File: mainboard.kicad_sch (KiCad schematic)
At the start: 0 parts

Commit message: schematic wip
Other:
- sheet CONTROL Port renamed USB
- added sheet Radio (radio.kicad_sch)
- sheet Clock and Miscellaneous ports: added AFE_CLK, FPGA_CLK, RX_MIX_CLK, RX_RCVR_CLK, TX_MIX_CLK, TX_XCVR_CLK; removed CLOCK_60MHZ
- sheet Debugger ports: added LED[1..3], MCU_D+, MCU_D-, USB_RESET_DETECT, USB_SWITCH; removed CONTROL_MCU_D+, CONTROL_MCU_D-, CONTROL_RESET_DETECT, CONTROL_SWITCH, LED[10..14]
- sheet Expansion Interfaces ports: added PMOD[1..10]; removed PMOD_A[0..7], PMOD_B[0..7]
- sheet FPGA Banks 0 and 1 ports: added 3V3RX_EN, AFE_ALT_CLK, AFE_SPI{SPI}, DA[0..7], DD[0..9], RX_MIX_CTRL{RFFC5072}, RX_RCVR{MAX2120}, ~{RX_MIX_BYPASS}; removed CLOCK_60MHZ, LED[0..5], MEZZANINE[1..30], PMOD_A[0..7], PMOD_B[0..7]
- sheet FPGA Banks 2 and 3 ports: added 3V3TX_EN, FPGA_CLK, LED[4..6], PHY{ULPI}, TX_MIX_CTRL{RFFC5072}, TX_XCVR{MAX2831}, ~{TX_MIX_BYPASS}; removed CONTROL_PHY{ULPI}, MEZZANINE[1..30], ~{BTN_USER}
- sheet FPGA Banks 6 and 7 ports: added MEZZANINE[1..30], PMOD[1..10], ~{BTN_USER}; removed none
- sheet LEDs and Buttons ports: added LED[1..3], LED[4..6]; removed LED[0..5], LED[10..14]
- sheet Power Supplies ports: added ~{POWER_GOOD}; removed none
- sheet USB: file control_port.kicad_sch -> usb.kicad_sch
- sheet USB ports: added MCU_D+, MCU_D-, PHY{ULPI}, USB_RESET_DETECT, USB_SWITCH; removed CONTROL_MCU_D+, CONTROL_MCU_D-, CONTROL_PHY{ULPI}, CONTROL_RESET_DETECT, CONTROL_SWITCH

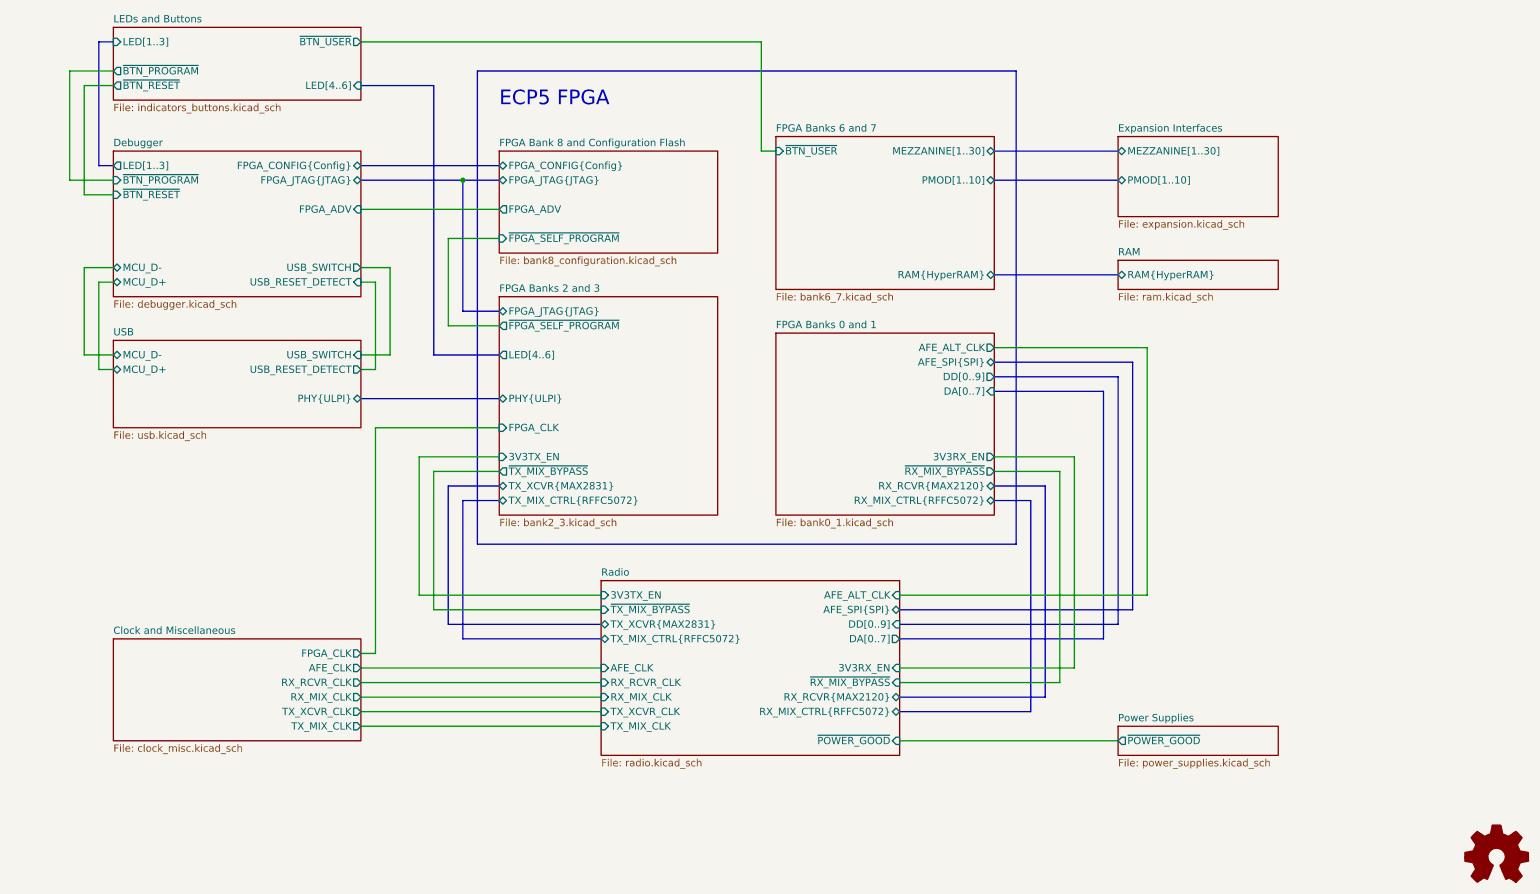
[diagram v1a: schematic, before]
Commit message: add regulator for analog 3.3 V supply
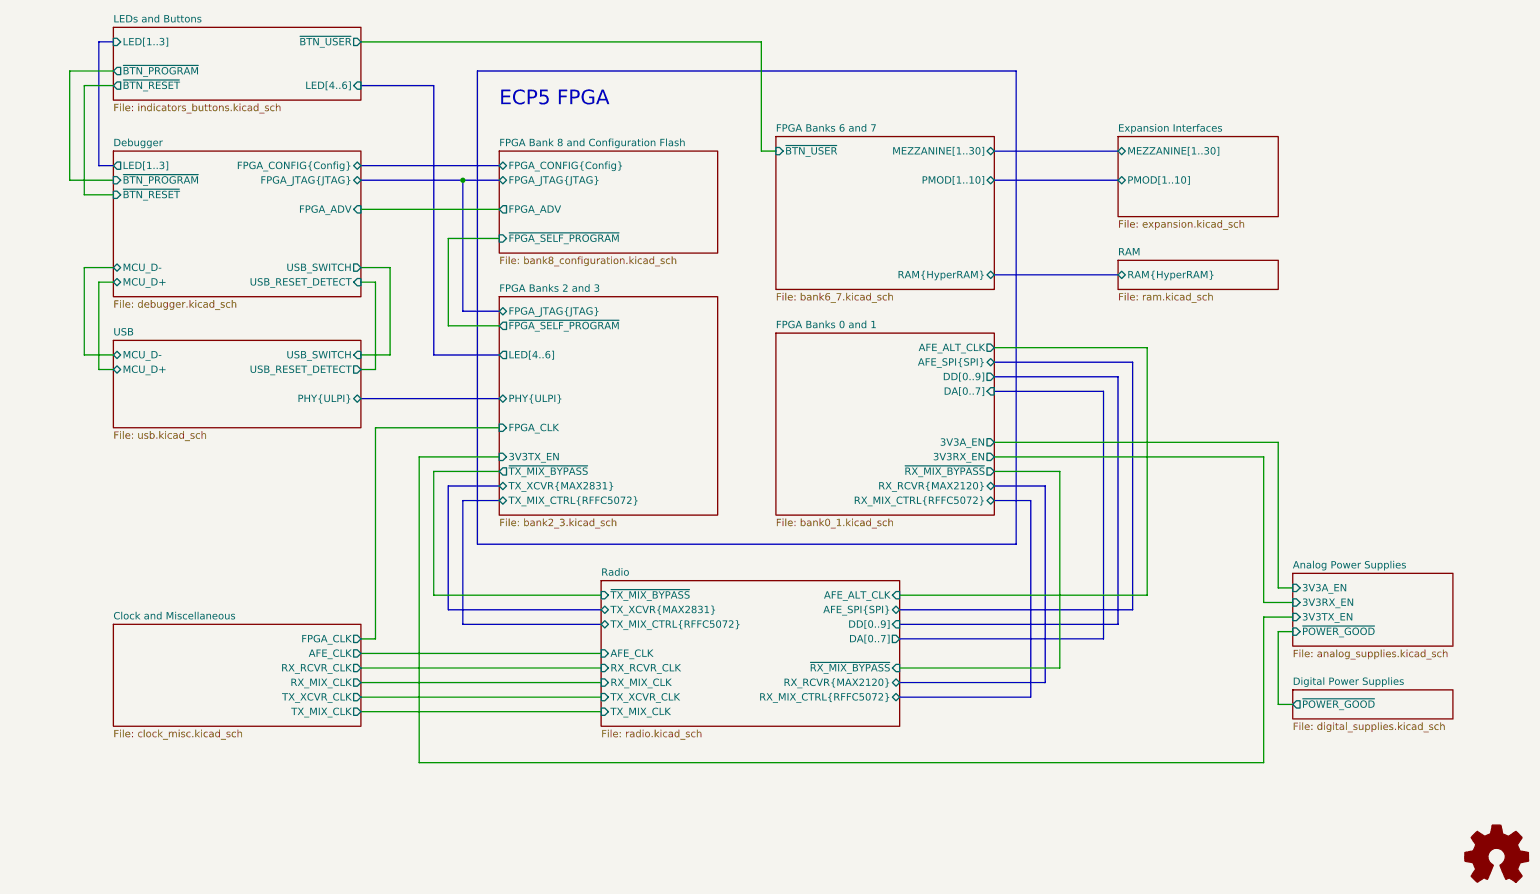
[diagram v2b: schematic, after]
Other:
- sheet Power Supplies renamed Digital Power Supplies
- added sheet Analog Power Supplies (analog_supplies.kicad_sch)
- sheet Digital Power Supplies: file power_supplies.kicad_sch -> digital_supplies.kicad_sch
- sheet FPGA Banks 0 and 1 ports: added 3V3A_EN; removed none
- sheet Radio ports: added none; removed 3V3RX_EN, 3V3TX_EN, ~{POWER_GOOD}

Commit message: complete initial layout
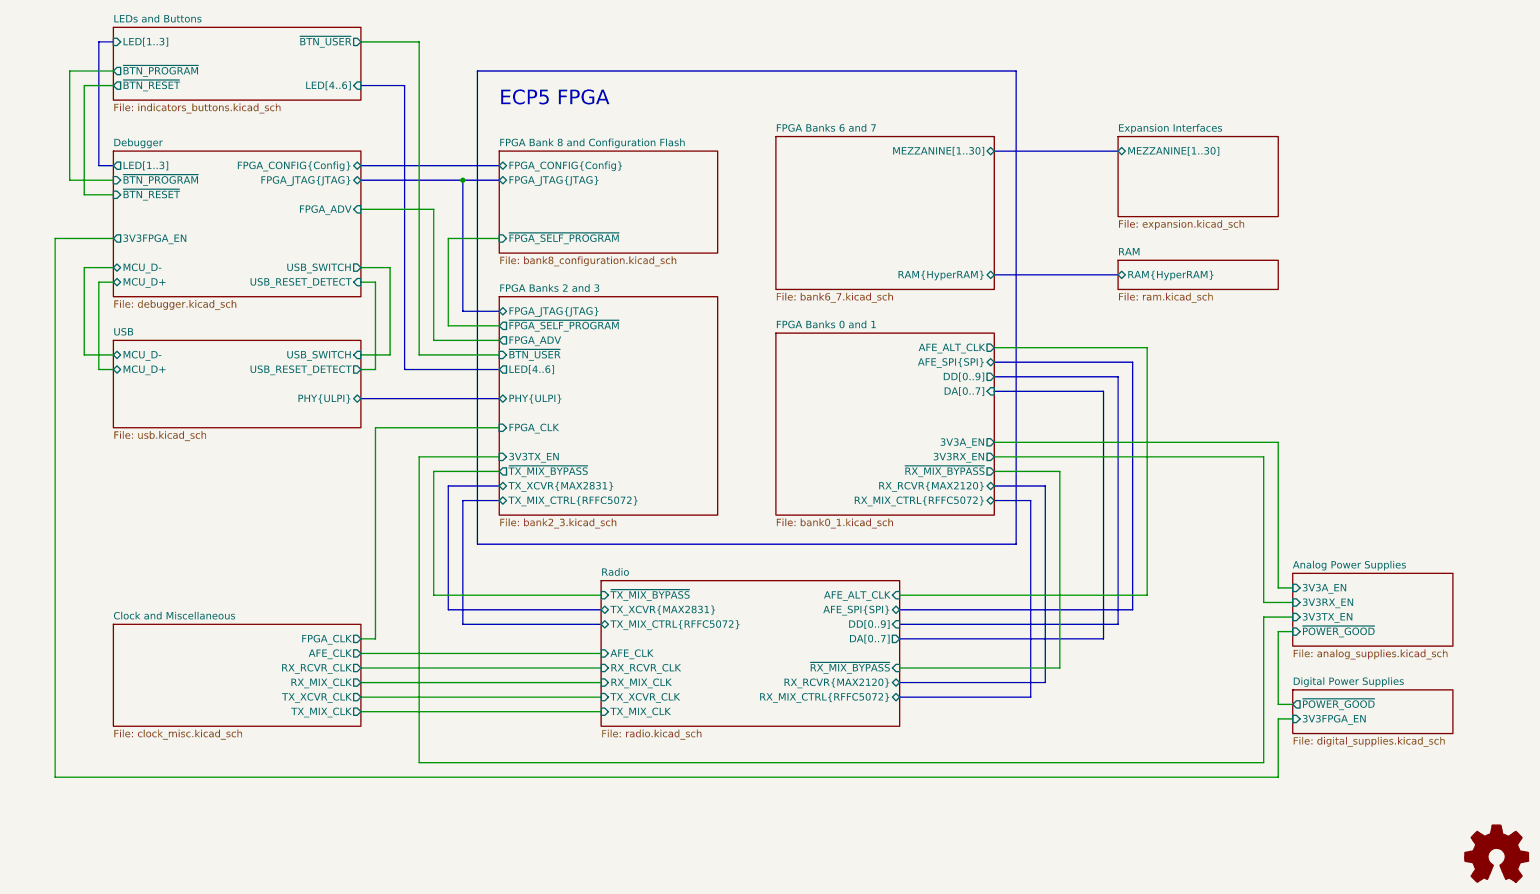
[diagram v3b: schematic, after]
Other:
- sheet Debugger ports: added 3V3FPGA_EN; removed none
- sheet Digital Power Supplies ports: added 3V3FPGA_EN; removed none
- sheet Expansion Interfaces ports: added none; removed PMOD[1..10]
- sheet FPGA Bank 8 and Configuration Flash ports: added none; removed FPGA_ADV
- sheet FPGA Banks 2 and 3 ports: added FPGA_ADV, ~{BTN_USER}; removed none
- sheet FPGA Banks 6 and 7 ports: added none; removed PMOD[1..10], ~{BTN_USER}
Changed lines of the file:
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@@
+    (stroke (width 0) (type default))
+  )
+  (wire (pts (xy 25.4 67.31) (xy 25.4 161.29))
     (stroke (width 0) (type default))
   )
@@
     (stroke (width 0) (type default))
   )
-  (wire (pts (xy 78.74 62.23) (xy 102.87 62.23))
-    (stroke (width 0) (type default))
-  )
   (bus (pts (xy 78.74 54.61) (xy 102.87 54.61))
     (stroke (width 0) (type default))
@@
     (stroke (width 0) (type default))
   )
+  (wire (pts (xy 78.74 33.02) (xy 88.9 33.02))
+    (stroke (width 0) (type default))
+  )
   (wire (pts (xy 189.23 107.95) (xy 200.66 107.95))
     (stroke (width 0) (type default))
   )
+  (wire (pts (xy 25.4 67.31) (xy 35.56 67.31))
+    (stroke (width 0) (type default))
+  )
   (wire (pts (xy 91.44 129.54) (xy 120.65 129.54))
     (stroke (width 0) (type default))
@@
     (stroke (width 0) (type default))
   )
+  (wire (pts (xy 91.44 62.23) (xy 78.74 62.23))
+    (stroke (width 0) (type default))
+  )
   (wire (pts (xy 33.02 74.93) (xy 33.02 90.17))
     (stroke (width 0) (type default))
@@
     (stroke (width 0) (type default))
   )
-  (wire (pts (xy 78.74 33.02) (xy 148.59 33.02))
-    (stroke (width 0) (type default))
-  )
   (bus (pts (xy 210.82 91.44) (xy 210.82 134.62))
     (stroke (width 0) (type default))
   )
+  (wire (pts (xy 238.76 161.29) (xy 25.4 161.29))
+    (stroke (width 0) (type default))
+  )
   (bus (pts (xy 93.98 132.08) (xy 120.65 132.08))
     (stroke (width 0) (type default))
   )
+  (wire (pts (xy 91.44 85.09) (xy 91.44 62.23))
+    (stroke (width 0) (type default))
+  )
   (bus (pts (xy 93.98 110.49) (xy 93.98 132.08))
     (stroke (width 0) (type default))
@@
     (stroke (width 0) (type default))
   )
+  (wire (pts (xy 241.3 151.13) (xy 238.76 151.13))
+    (stroke (width 0) (type default))
+  )
   (wire (pts (xy 189.23 105.41) (xy 236.22 105.41))
     (stroke (width 0) (type default))
@@
     (stroke (width 0) (type default))
   )
-  (bus (pts (xy 189.23 57.15) (xy 210.82 57.15))
-    (stroke (width 0) (type default))
-  )
   (wire (pts (xy 102.87 67.31) (xy 93.98 67.31))
     (stroke (width 0) (type default))
   )
-  (wire (pts (xy 148.59 33.02) (xy 148.59 52.07))
-    (stroke (width 0) (type default))
-  )
   (bus (pts (xy 213.36 88.9) (xy 213.36 132.08))
     (stroke (width 0) (type default))
@@
     (stroke (width 0) (type default))
   )
-  (bus (pts (xy 78.74 40.64) (xy 91.44 40.64))
-    (stroke (width 0) (type default))
-  )
-  (wire (pts (xy 148.59 52.07) (xy 151.13 52.07))
+  (wire (pts (xy 88.9 33.02) (xy 88.9 87.63))
+    (stroke (width 0) (type default))
+  )
+  (bus (pts (xy 78.74 40.64) (xy 86.36 40.64))
+    (stroke (width 0) (type default))
+  )
+  (wire (pts (xy 88.9 87.63) (xy 102.87 87.63))
     (stroke (width 0) (type default))
   )
@@
     (stroke (width 0) (type default))
   )
+  (wire (pts (xy 102.87 85.09) (xy 91.44 85.09))
+    (stroke (width 0) (type default))
+  )
   (wire (pts (xy 241.3 135.89) (xy 238.76 135.89))
     (stroke (width 0) (type default))
@@
     (stroke (width 0) (type default))
   )
-  (bus (pts (xy 102.87 87.63) (xy 91.44 87.63))
+  (bus (pts (xy 102.87 90.17) (xy 86.36 90.17))
     (stroke (width 0) (type default))
   )
@@
     (stroke (width 0) (type default))
   )
-  (bus (pts (xy 91.44 87.63) (xy 91.44 40.64))
+  (bus (pts (xy 86.36 90.17) (xy 86.36 40.64))
     (stroke (width 0) (type default))
   )
@@
   )
   (wire (pts (xy 78.74 142.24) (xy 120.65 142.24))
+    (stroke (width 0) (type default))
+  )
+  (wire (pts (xy 238.76 151.13) (xy 238.76 161.29))
     (stroke (width 0) (type default))
   )
@@
     )
   )
-  (sheet (at 241.3 146.05) (size 27.94 5.08) (fields_autoplaced)
+  (sheet (at 241.3 146.05) (size 27.94 7.62) (fields_autoplaced)
     (stroke (width 0) (type solid))
     (fill (color 0 0 0 0.0000))
@@
       (effects (font (size 1.27 1.27)) (justify left bottom))
     )
-    (property "Sheetfile" "digital_supplies.kicad_sch" (at 241.3 151.7146 0)
+    (property "Sheetfile" "digital_supplies.kicad_sch" (at 241.3 154.2546 0)
       (effects (font (size 1.27 1.27)) (justify left top))
     )
@@
       (effects (font (size 1.27 1.27)) (justify left))
     )
+    (pin "3V3FPGA_EN" input (at 241.3 151.13 180)
+      (effects (font (size 1.27 1.27)) (justify left))
+    )
     (instances
       (project "mainboard"
@@
     )
     (pin "LED[1..3]" output (at 35.56 54.61 180)
+      (effects (font (size 1.27 1.27)) (justify left))
+    )
+    (pin "3V3FPGA_EN" output (at 35.56 67.31 180)
       (effects (font (size 1.27 1.27)) (justify left))
     )
@@
       (effects (font (size 1.27 1.27)) (justify right))
     )
-    (pin "~{BTN_USER}" input (at 151.13 52.07 180)
-      (effects (font (size 1.27 1.27)) (justify left))
-    )
-    (pin "PMOD[1..10]" bidirectional (at 189.23 57.15 0)
-      (effects (font (size 1.27 1.27)) (justify right))
-    )
     (instances
       (project "mainboard"
@@
       (effects (font (size 1.27 1.27)) (justify left))
     )
-    (pin "LED[4..6]" output (at 102.87 87.63 180)
+    (pin "LED[4..6]" output (at 102.87 90.17 180)
       (effects (font (size 1.27 1.27)) (justify left))
     )
     (pin "~{TX_MIX_BYPASS}" output (at 102.87 107.95 180)
+      (effects (font (size 1.27 1.27)) (justify left))
+    )
+    (pin "FPGA_ADV" output (at 102.87 85.09 180)
+      (effects (font (size 1.27 1.27)) (justify left))
+    )
+    (pin "~{BTN_USER}" input (at 102.87 87.63 180)
       (effects (font (size 1.27 1.27)) (justify left))
     )
@@
       (effects (font (size 1.27 1.27)) (justify left))
     )
-    (pin "PMOD[1..10]" bidirectional (at 210.82 57.15 180)
-      (effects (font (size 1.27 1.27)) (justify left))
-    )
     (instances
       (project "mainboard"
@@
       (effects (font (size 1.27 1.27)) (justify left))
     )
-    (pin "FPGA_ADV" output (at 102.87 62.23 180)
-      (effects (font (size 1.27 1.27)) (justify left))
-    )

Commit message: invert 3V3FPGA_EN
The mcu has default pull-up, not pull-down.
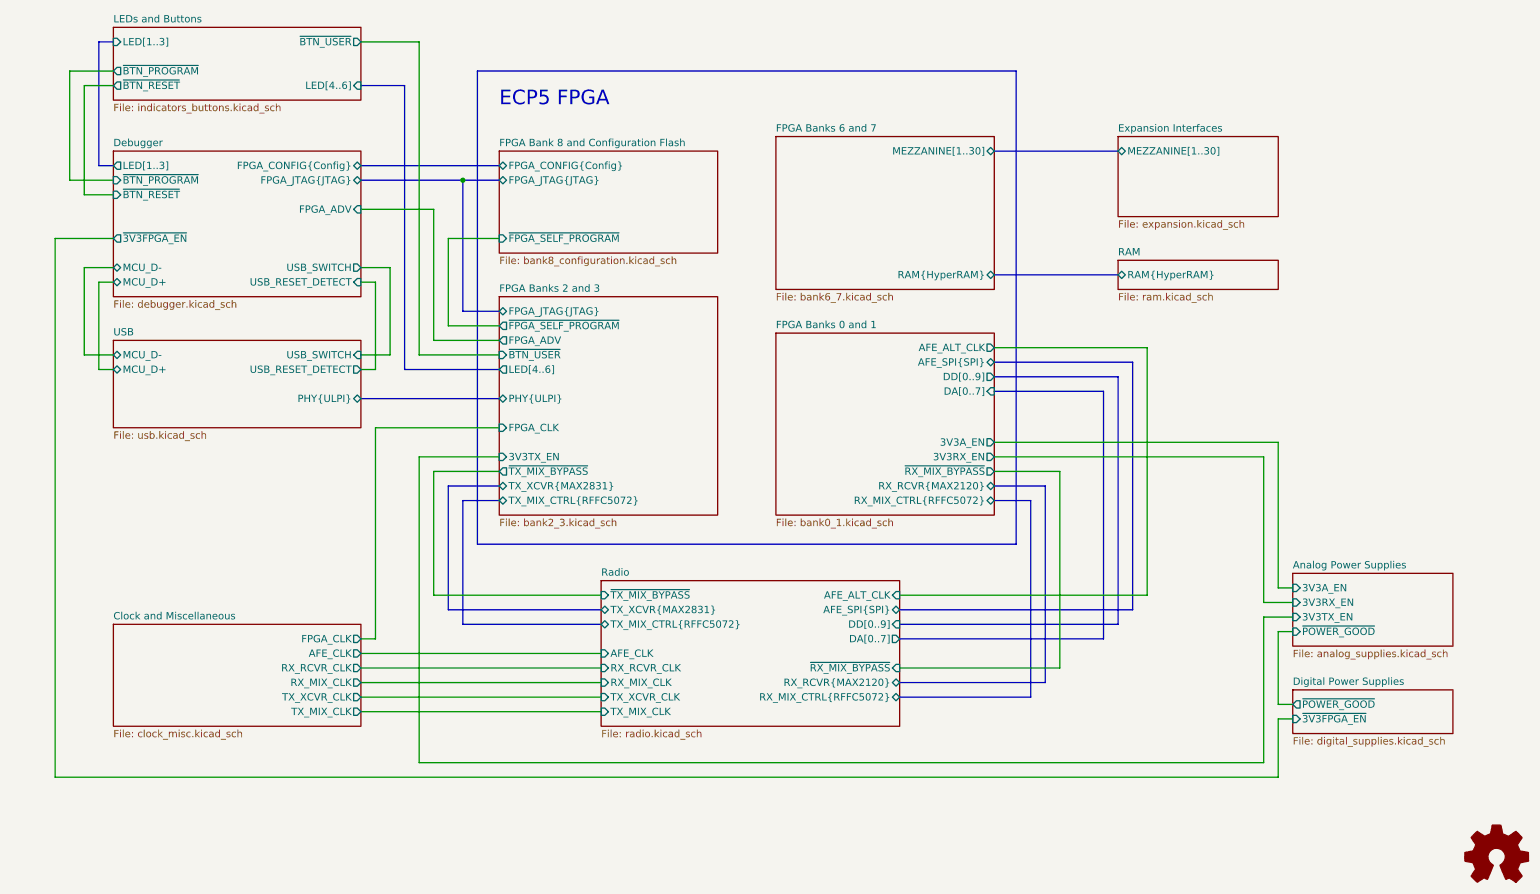
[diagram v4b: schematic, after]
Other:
- sheet Debugger ports: added ~{3V3FPGA_EN}; removed 3V3FPGA_EN
- sheet Digital Power Supplies ports: added ~{3V3FPGA_EN}; removed 3V3FPGA_EN
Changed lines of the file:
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@@
       (effects (font (size 1.27 1.27)) (justify left))
     )
-    (pin "3V3FPGA_EN" input (at 241.3 151.13 180)
+    (pin "~{3V3FPGA_EN}" input (at 241.3 151.13 180)
       (effects (font (size 1.27 1.27)) (justify left))
     )
@@
       (effects (font (size 1.27 1.27)) (justify left))
     )
-    (pin "3V3FPGA_EN" output (at 35.56 67.31 180)
+    (pin "~{3V3FPGA_EN}" output (at 35.56 67.31 180)
       (effects (font (size 1.27 1.27)) (justify left))
     )
